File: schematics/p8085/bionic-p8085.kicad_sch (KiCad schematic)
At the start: 4 parts, among them J1 BionicConnector, U1 MSM80C85AH, U2 74HCT126

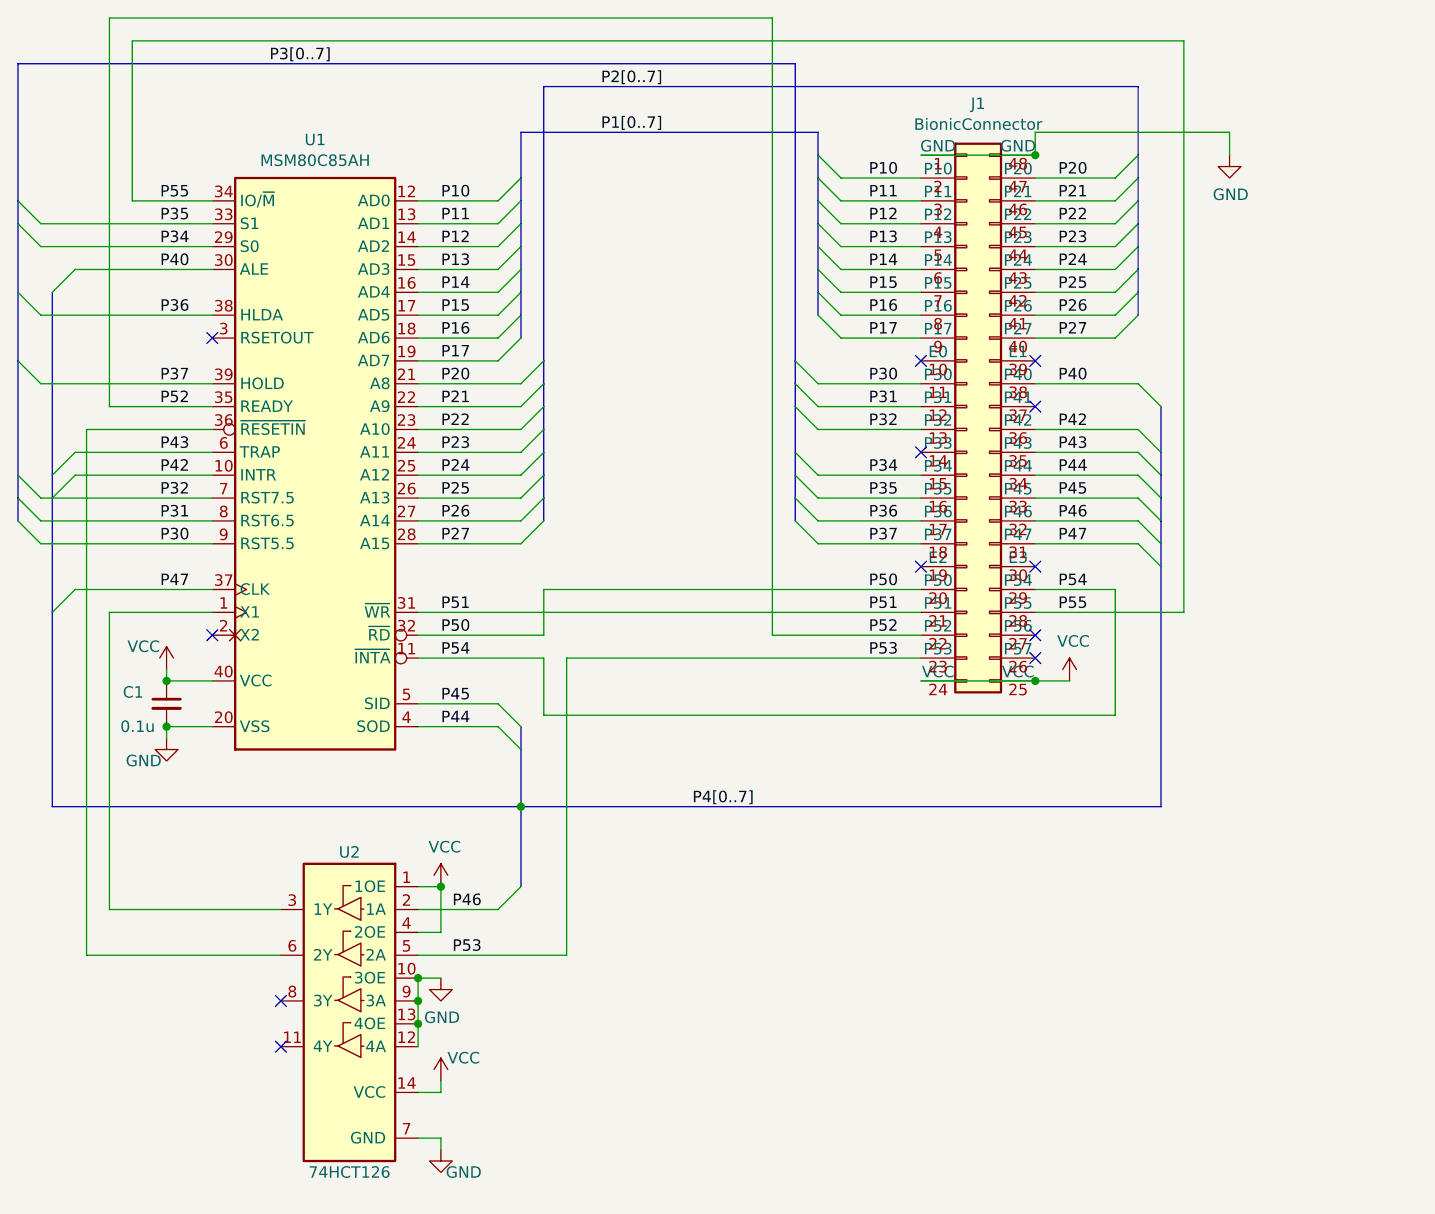
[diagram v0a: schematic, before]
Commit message: [P8085] Move schematics directory
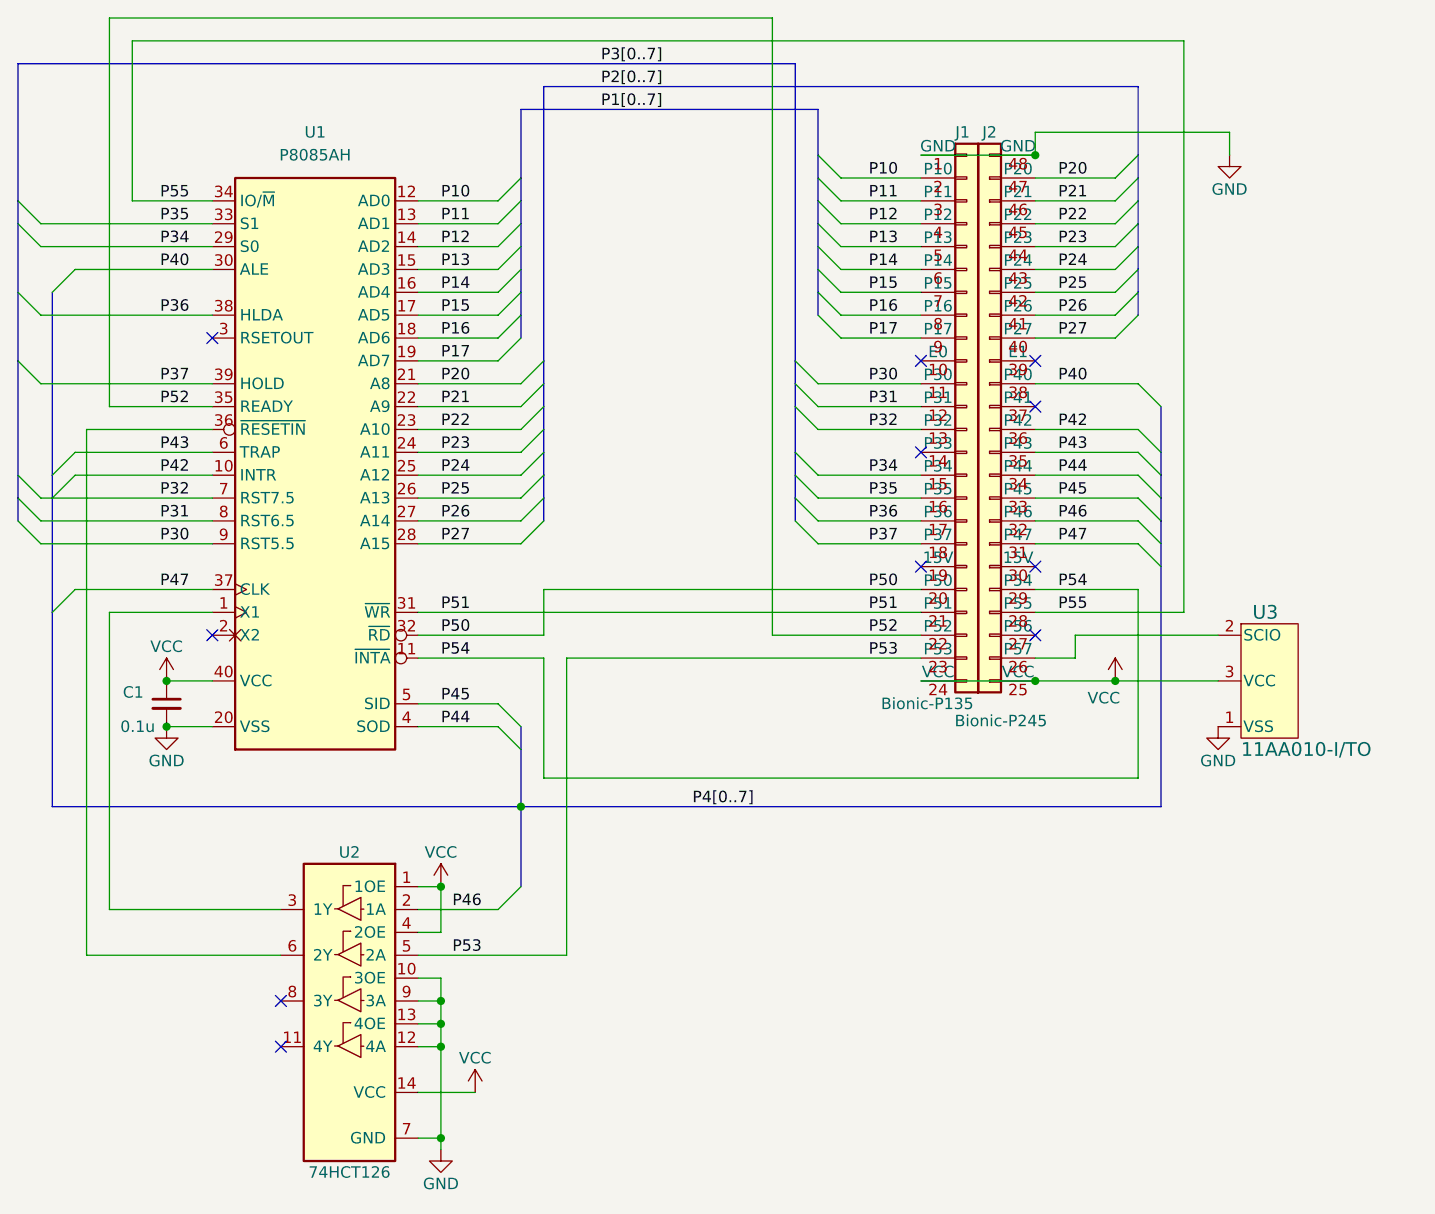
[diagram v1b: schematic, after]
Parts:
- removed J1: BionicConnector, 0-LocalLibrary:DIP-48_W7.62mm, symbol 0-LocalLibrary:BionicConnector
- removed U1: MSM80C85AH, Package_DIP:DIP-40_W15.24mm, symbol 0-LocalLibrary:MSM80C85AH
- added J1: Bionic-P135, connector:Bionic-P135_Vertical, symbol 0-LocalLibrary:Bionic-P135
- added J2: Bionic-P245, connector:Bionic-P245_Vertical, symbol 0-LocalLibrary:Bionic-P245
- added U1: P8085AH, Package_DIP:DIP-40_W15.24mm, symbol 0-LocalLibrary:P8085AH
- added U3: 11AA010-I/TO, TO-92_MC_MCH, symbol 0-LocalLibrary:11AA010-I_TO
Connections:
- net GND: now also J1.1 (GND), J2.48 (GND), U1.20 (VSS), U3.1 (VSS)
- net P10: now also J1.2 (P10), U1.12 (AD0)
- net P11: now also J1.3 (P11), U1.13 (AD1)
- net P12: now also J1.4 (P12), U1.14 (AD2)
- net P13: now also J1.5 (P13), U1.15 (AD3)
- net P14: now also J1.6 (P14), U1.16 (AD4)
- net P15: now also J1.7 (P15), U1.17 (AD5)
- net P16: now also J1.8 (P16), U1.18 (AD6)
- net P17: now also J1.9 (P17), U1.19 (AD7)
- net P20: now also J2.47 (P20), U1.21 (A8)
- net P21: now also J2.46 (P21), U1.22 (A9)
- net P22: now also J2.45 (P22), U1.23 (A10)
- net P23: now also J2.44 (P23), U1.24 (A11)
- net P24: now also J2.43 (P24), U1.25 (A12)
- net P25: now also J2.42 (P25), U1.26 (A13)
- net P26: now also J2.41 (P26), U1.27 (A14)
- net P27: now also J2.40 (P27), U1.28 (A15)
- net P30: now also J1.11 (P30), U1.9 (RST5.5)
- net P31: now also J1.12 (P31), U1.8 (RST6.5)
- net P32: now also J1.13 (P32), U1.7 (RST7.5)
- net P34: now also J1.15 (P34), U1.29 (S0)
- net P35: now also J1.16 (P35), U1.33 (S1)
- net P36: now also J1.17 (P36), U1.38 (HLDA)
- net P37: now also J1.18 (P37), U1.39 (HOLD)
- net P40: now also J2.38 (P40), U1.30 (ALE)
- net P42: now also J2.36 (P42), U1.10 (INTR)
- net P43: now also J2.35 (P43), U1.6 (TRAP)
- net P44: now also J2.34 (P44), U1.4 (SOD)
- net P45: now also J2.33 (P45), U1.5 (SID)
- net P46: now also J2.32 (P46)
- net P47: now also J2.31 (P47), U1.37 (CLK)
- net P50: now also J1.20 (P50), U1.32 (~{RD})
- net P51: now also J1.21 (P51), U1.31 (~{WR})
- net P52: now also J1.22 (P52), U1.35 (READY)
- net P53: now also J1.23 (P53)
- net P54: now also J2.29 (P54), U1.11 (~{INTA})
- net P55: now also J2.28 (P55), U1.34 (IO/~{M})
- net VCC: now also J1.24 (VCC), J2.25 (VCC), U1.40 (VCC), U3.3 (VCC)
- net at U2.3 (1Y): now also U1.1 (X1)
- net at U2.6 (2Y): now also U1.36 (~{RESETIN})
- new net: J2.26 (P57), U3.2 (SCIO)
- no-connect marks 12 -> 11
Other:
- title: BionicP8085 Mezzanine -> BionicP8085

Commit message: [P8085] Remove HC126
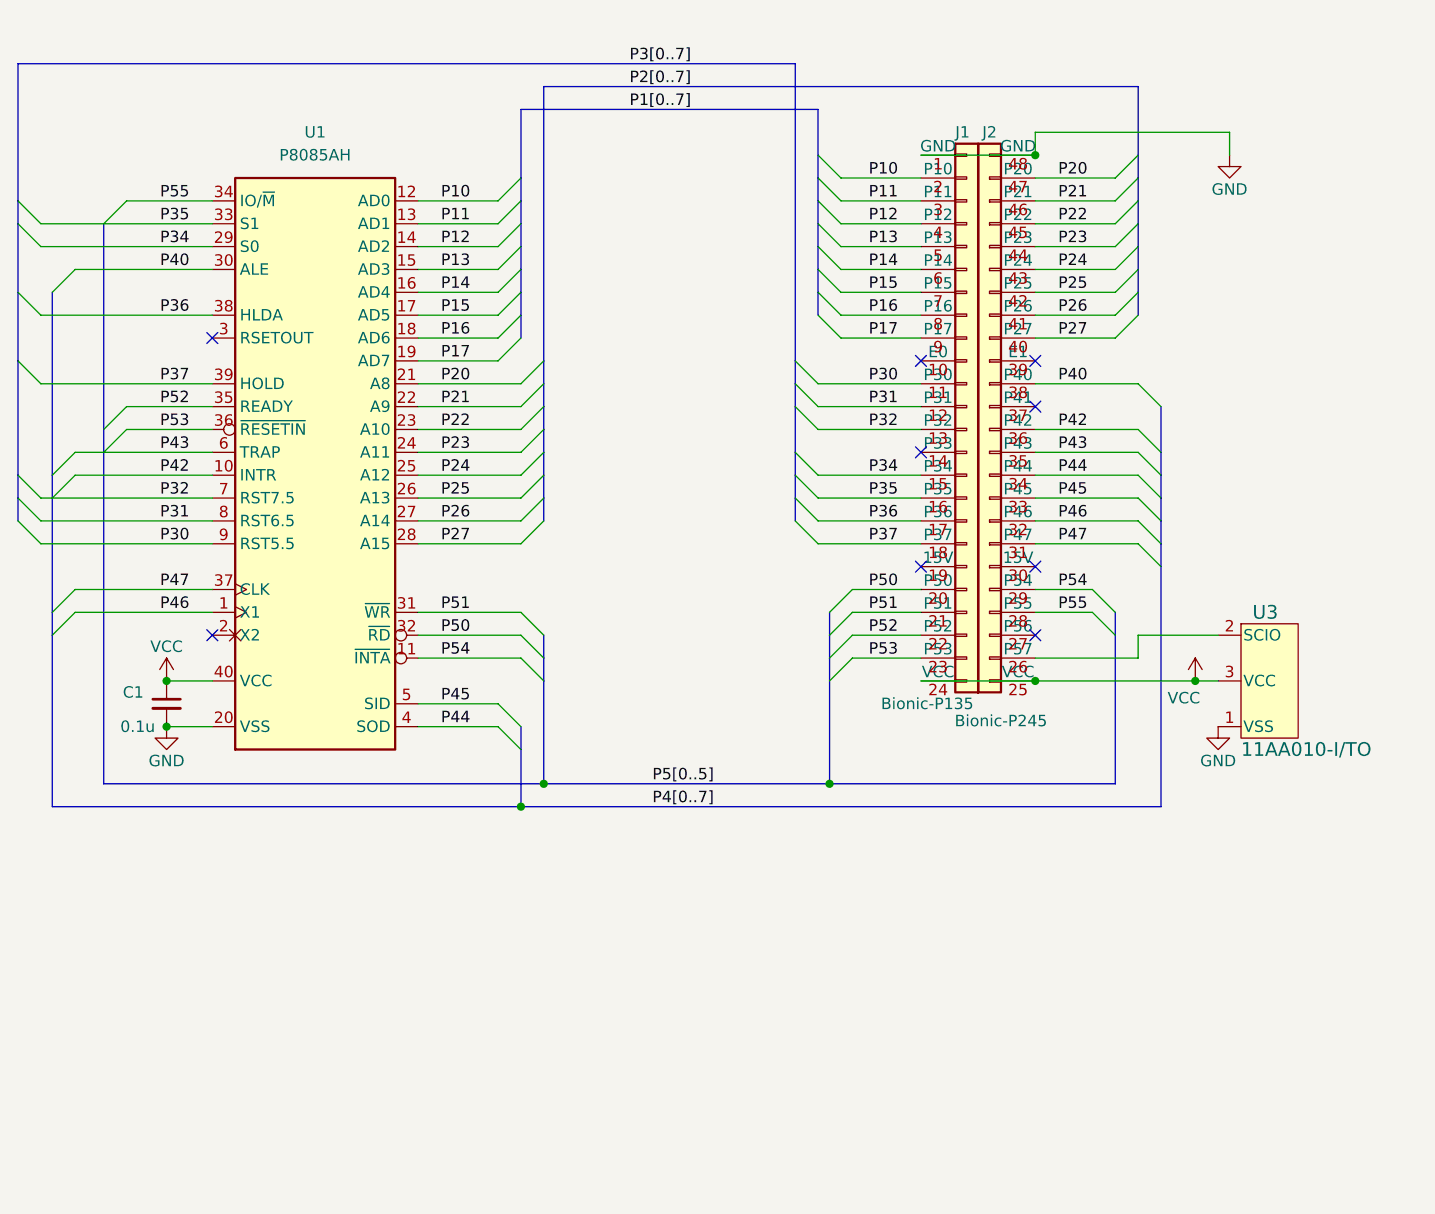
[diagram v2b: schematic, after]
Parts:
- removed U2: 74HCT126, Package_DIP:DIP-14_W7.62mm, symbol 0-LocalLibrary:74HCT126
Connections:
- net P46: now also U1.1 (X1)
- net P53: now also U1.36 (~{RESETIN})
- no-connect marks 11 -> 9
